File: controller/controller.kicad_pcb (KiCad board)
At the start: 2 copper layers, 8 parts, among them SW1 Move Up Btn, SW2 Move Down Btn, SW3 Move Right Btn, SW4 Move Left Btn, SW5 Attack Btn, SW6 Defense Btn

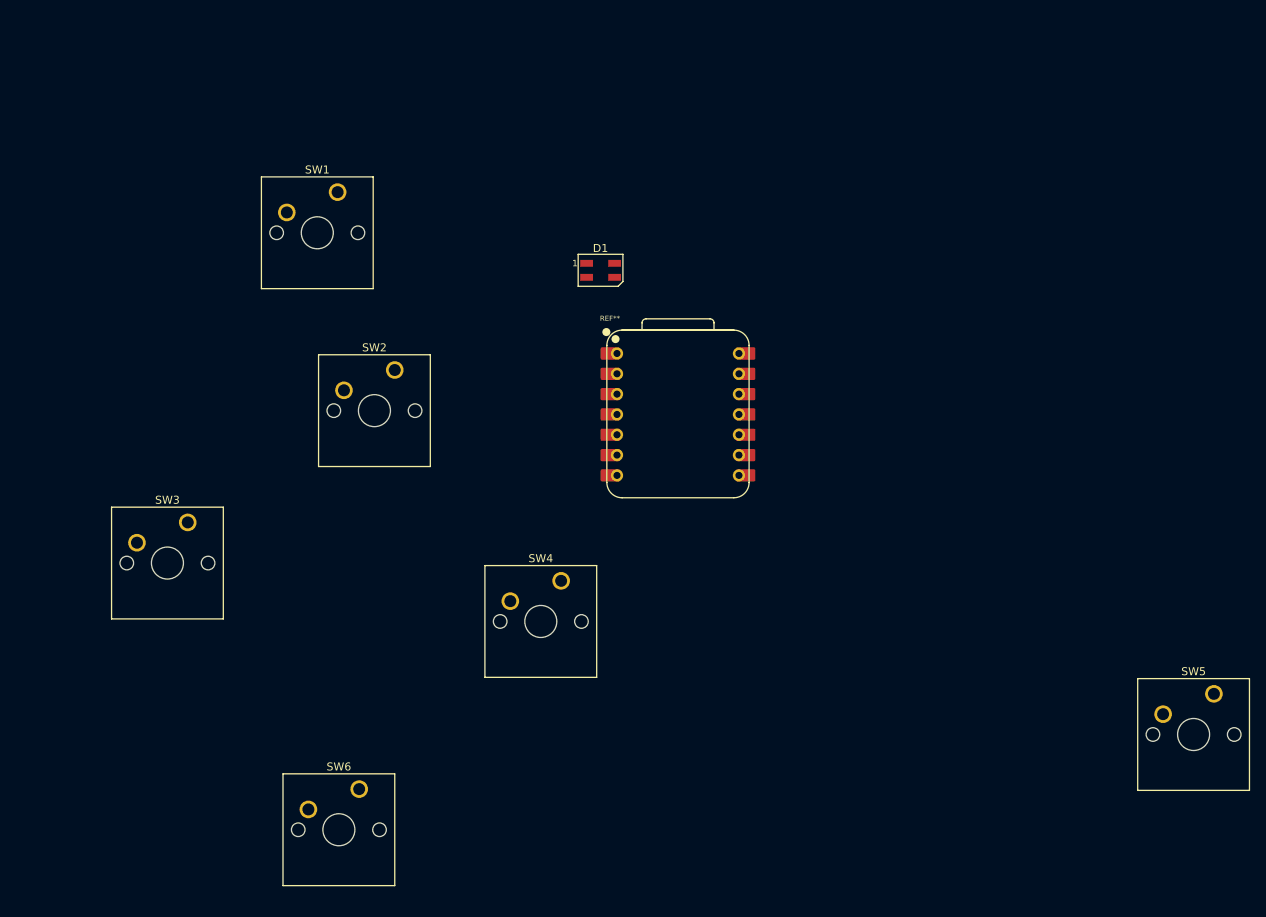
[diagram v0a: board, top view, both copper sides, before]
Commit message: SO I have Started and finsihed the PCb. I had to assign all the footprint to all the components in the schematic editor. Then After Importing them I had to import a Graphic Picture of Controller Outline. SO I put all the componenets in the controller outline. Then I started all the componenets with each other (Although I forgot to reimport the microcontroller because it did not had labels). I have Connected all the Data Pins and Vcc Pins on the front (with one exception) and all the Ground Pins on the Back SIde. I Have Connected the LED with the resistor and then second end with Ground. The Resistor is Directy COnnected with the VCC. Now I am Only facing One Problem which is that there is a small gap in my controller outline because of which the kicad is not abe to properly cut the pcb into my desired shape.
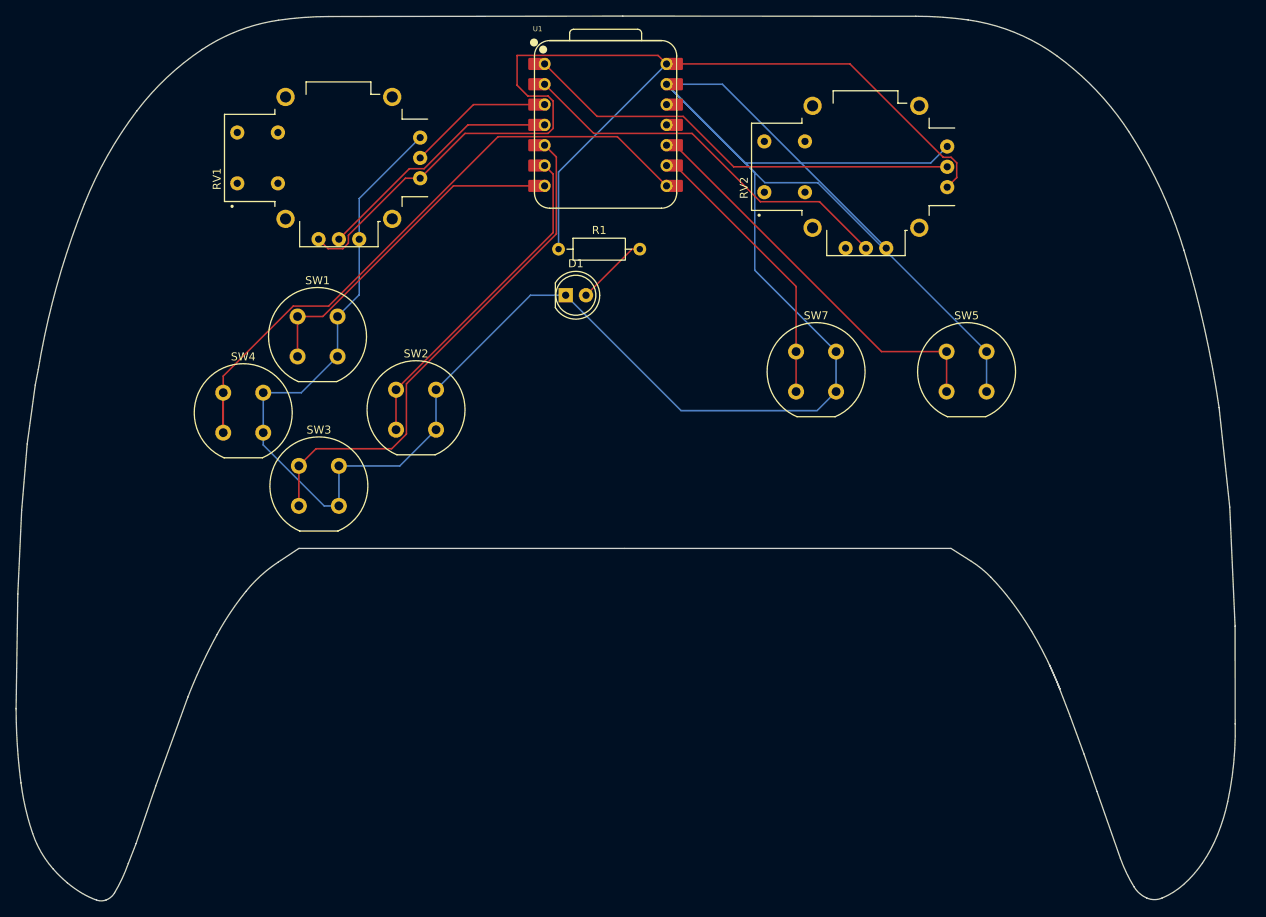
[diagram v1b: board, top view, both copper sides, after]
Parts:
- removed REF**: XIAO-RP2040-DIP, OPL:XIAO-RP2040-DIP
- removed SW6: Defense Btn, Button_Switch_Keyboard:SW_Cherry_MX_1.00u_PCB
- added R1: R, Resistor_THT:R_Axial_DIN0207_L6.3mm_D2.5mm_P10.16mm_Horizontal, F.Cu at (175.1, 48.9)
- added RV1: Left Stick, Joystick:XDCR_COM-09032, F.Cu at (147.6, 37.5)
- added RV2: Rigth Stick, Joystick:XDCR_COM-09032, F.Cu at (213.5, 38.6)
- added SW7: Attack Btn, Button_Switch_THT:Push_E-Switch_KS01Q01, F.Cu at (204.8, 61.7)
- added U1: XIAO-RP2040-DIP, OPL_Kicad:XIAO-RP2040-DIP, F.Cu at (181.0, 33.3)
- D1: value SK6812MINI -> LED; footprint LED_SMD:LED_SK6812MINI_PLCC4_3.5x3.5mm_P1.75mm -> LED_THT:LED_D5.0mm
- SW1, SW4: footprint Button_Switch_Keyboard:SW_Cherry_MX_1.00u_PCB -> Button_Switch_THT:Push_E-Switch_KS01Q01
- SW2: value Move Down Btn -> Move Right Btn; footprint Button_Switch_Keyboard:SW_Cherry_MX_1.00u_PCB -> Button_Switch_THT:Push_E-Switch_KS01Q01
- SW3: value Move Right Btn -> Move Down Btn; footprint Button_Switch_Keyboard:SW_Cherry_MX_1.00u_PCB -> Button_Switch_THT:Push_E-Switch_KS01Q01
- SW5: value Attack Btn -> Defense Btn; footprint Button_Switch_Keyboard:SW_Cherry_MX_1.00u_PCB -> Button_Switch_THT:Push_E-Switch_KS01Q01
- moved SW5 54.3 mm to (223.6, 61.7)
- moved SW4 48.3 mm to (133.2, 66.8)
- moved SW1 16.3 mm to (142.5, 57.3)
- moved SW3 15.6 mm to (142.6, 76.0)
- moved D1 5.36 mm to (176.0, 54.6)
- moved SW2 2.47 mm to (154.8, 66.4)
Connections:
- D1 pad 1: unconnected-(D1-DOUT-Pad1) -> /GND
- D1 pad 2: unconnected-(D1-VSS-Pad2) -> Net-(D1-A)
- SW1 pad 1: unconnected-(SW1-Pad1) -> /D0
- SW1 pad 2: unconnected-(SW1-Pad2) -> /GND
- SW2 pad 1: unconnected-(SW2-Pad1) -> /D7
- SW2 pad 2: unconnected-(SW2-Pad2) -> /GND
- SW3 pad 1: unconnected-(SW3-Pad1) -> /D6
- SW3 pad 2: unconnected-(SW3-Pad2) -> /GND
- SW4 pad 1: unconnected-(SW4-Pad1) -> /D1
- SW4 pad 2: unconnected-(SW4-Pad2) -> /GND
- SW5 pad 1: unconnected-(SW5-Pad1) -> /D4
- SW5 pad 2: unconnected-(SW5-Pad2) -> /GND
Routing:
- net /GND: track 0.00 -> 330.1 mm
- net /VCC: track 0.00 -> 141.9 mm
- net /D1: track 0.00 -> 82.5 mm
- net /D6: track 0.00 -> 64.6 mm
- net /A0: track 0.00 -> 55.7 mm
- net /D4: track 0.00 -> 50.9 mm
- net /A1: track 0.00 -> 48.6 mm
- net /D0: track 0.00 -> 42.7 mm
- net /D7: track 0.00 -> 41.6 mm
- net /D2: track 0.00 -> 35.6 mm
- net /A3: track 0.00 -> 31.6 mm
- net /A2: track 0.00 -> 18.3 mm
- net Net-(D1-A): track 0.00 -> 9.12 mm
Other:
- board outline added: 152.4 x 110.6 mm
